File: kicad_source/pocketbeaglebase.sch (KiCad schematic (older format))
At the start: 13 parts, among them P4 CONN_02X20, P7 CONN_01X04, P8 CONN_02X03, U1 BEAGLE_PocketBeagle

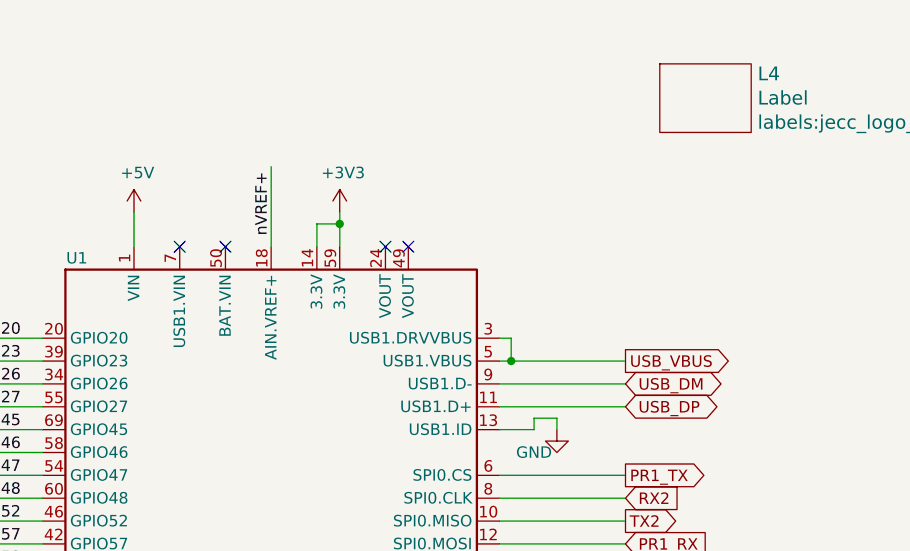
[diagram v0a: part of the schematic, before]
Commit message: tested and fixed last bugs
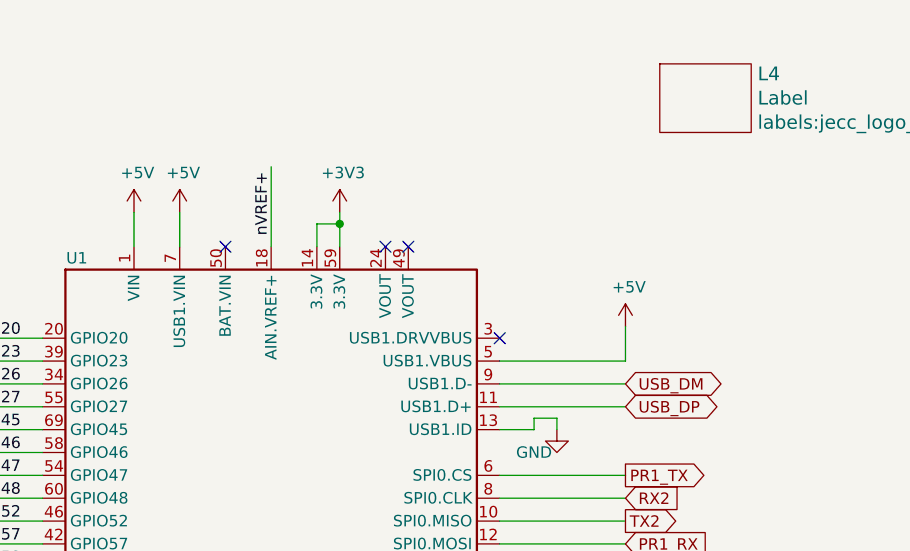
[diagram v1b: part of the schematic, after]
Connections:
- net +5V: now also U1.5 (USB1.VBUS), U1.7 (USB1.VIN)
- net USB_VBUS: no longer names the net of U1.3 (USB1.DRVVBUS)
- net USB_VBUS: no longer U1.5 (USB1.VBUS)
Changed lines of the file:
@@
 Wire Wire Line
 	4050 2450 4050 2500
-Wire Wire Line
-	3800 2100 3850 2100
-Wire Wire Line
-	3850 2100 3850 2200
-Wire Wire Line
-	3850 2200 3800 2200
-Wire Wire Line
-	3850 2200 4350 2200
-Connection ~ 3850 2200
-Text GLabel 4350 2200 2    50   Output ~ 0
-USB_VBUS
 $Sheet
 S 9300 2050 1600 1000
@@
 NoConn ~ 3300 1700
 NoConn ~ 2600 1700
-NoConn ~ 2400 1700
 $Comp
 L pocketbeaglebase-rescue:BEAGLE_PocketBeagle-MODULE_compute U1
@@
 	1    0    0    -1
 $EndComp
+Wire Wire Line
+	2400 1700 2400 1550
+Wire Wire Line
+	3800 2200 4350 2200
+NoConn ~ 3800 2100
+$Comp
+L power-supply:+5V #PWR?
+U 1 1 5FF01AE1
+P 2400 1550
+F 0 "#PWR?" H 2400 1400 50  0001 C CNN
+F 1 "+5V" H 2415 1723 50  0000 C CNN
+F 2 "" H 2400 1550 50  0000 C CNN
+F 3 "" H 2400 1550 50  0000 C CNN
+	1    2400 1550
+	1    0    0    -1
+$EndComp
+Wire Wire Line
+	4350 2200 4350 2050
+$Comp
+L power-supply:+5V #PWR?
+U 1 1 5FF0FE5A
+P 4350 2050
+F 0 "#PWR?" H 4350 1900 50  0001 C CNN
+F 1 "+5V" H 4365 2223 50  0000 C CNN
+F 2 "" H 4350 2050 50  0000 C CNN
+F 3 "" H 4350 2050 50  0000 C CNN
+	1    4350 2050
+	1    0    0    -1
+$EndComp
